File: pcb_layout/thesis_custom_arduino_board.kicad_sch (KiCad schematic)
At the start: 36 parts, among them J1 POWER, J2 USB to TTL, J3 ICSP, J4 VSupply, J5 6-channel Relay, J6 VSupply, J7 Light Sensor, J8 I2C Device, J9 RPi Connector, M1 TXB0104, M2 TB6612FNG, M3 GY-906-BCC, M4 JSN-SR04T, SW1 Reset SW, U1 ATmega328P-P, U2 LM7805, U3 LM317, Y1 16MHz

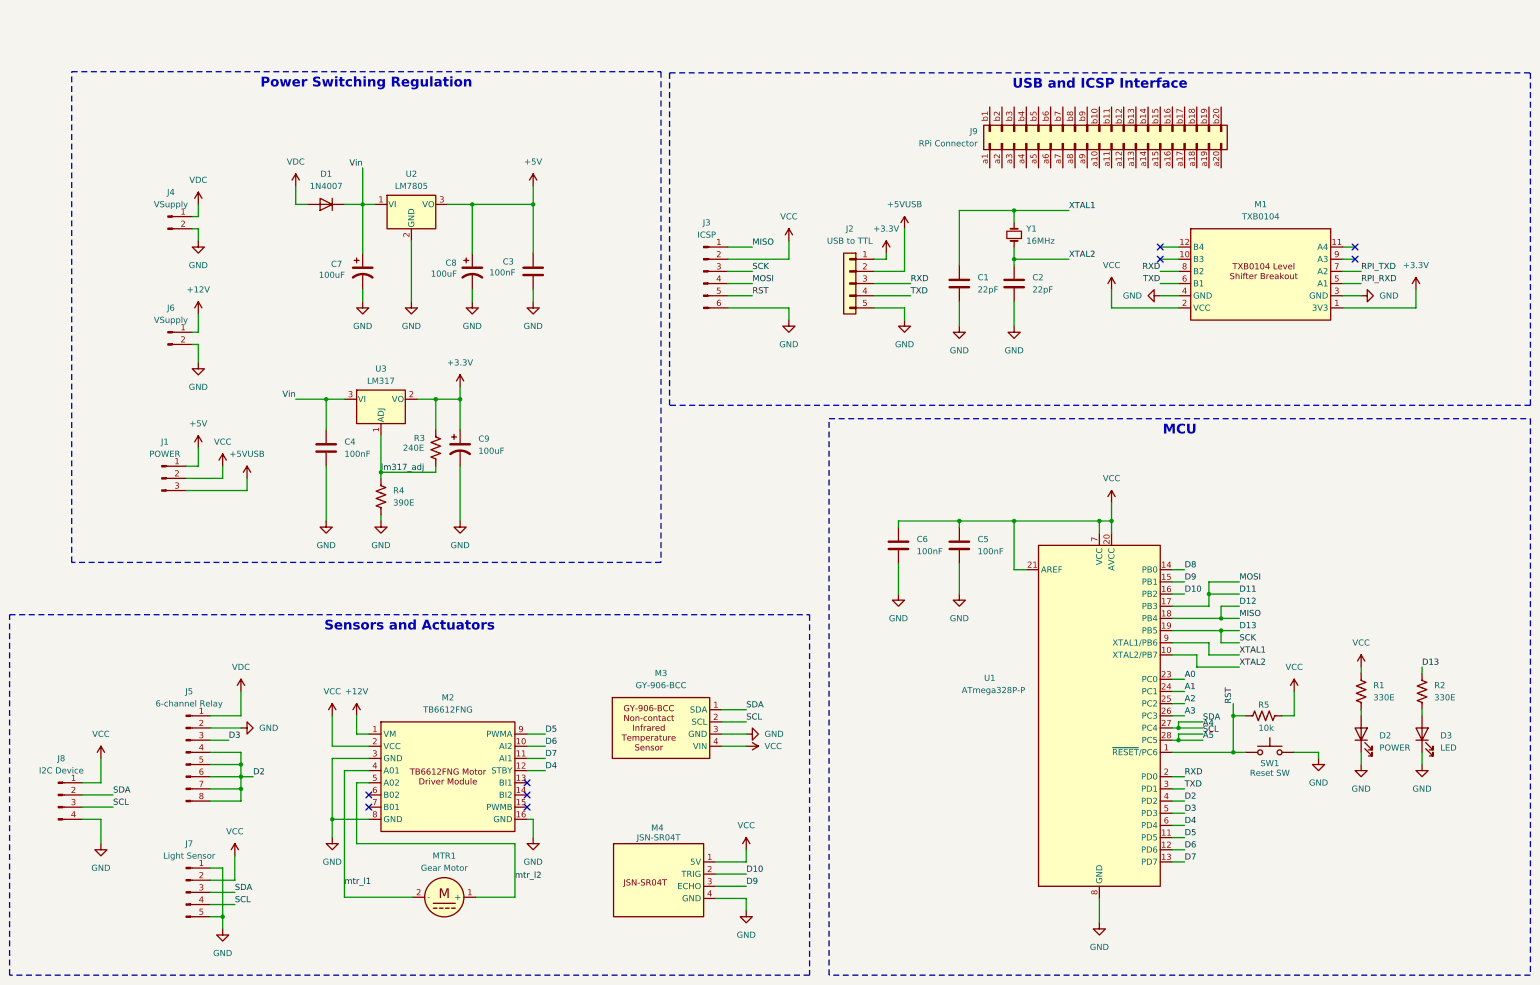
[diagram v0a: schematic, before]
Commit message: Added: Line detector module pins
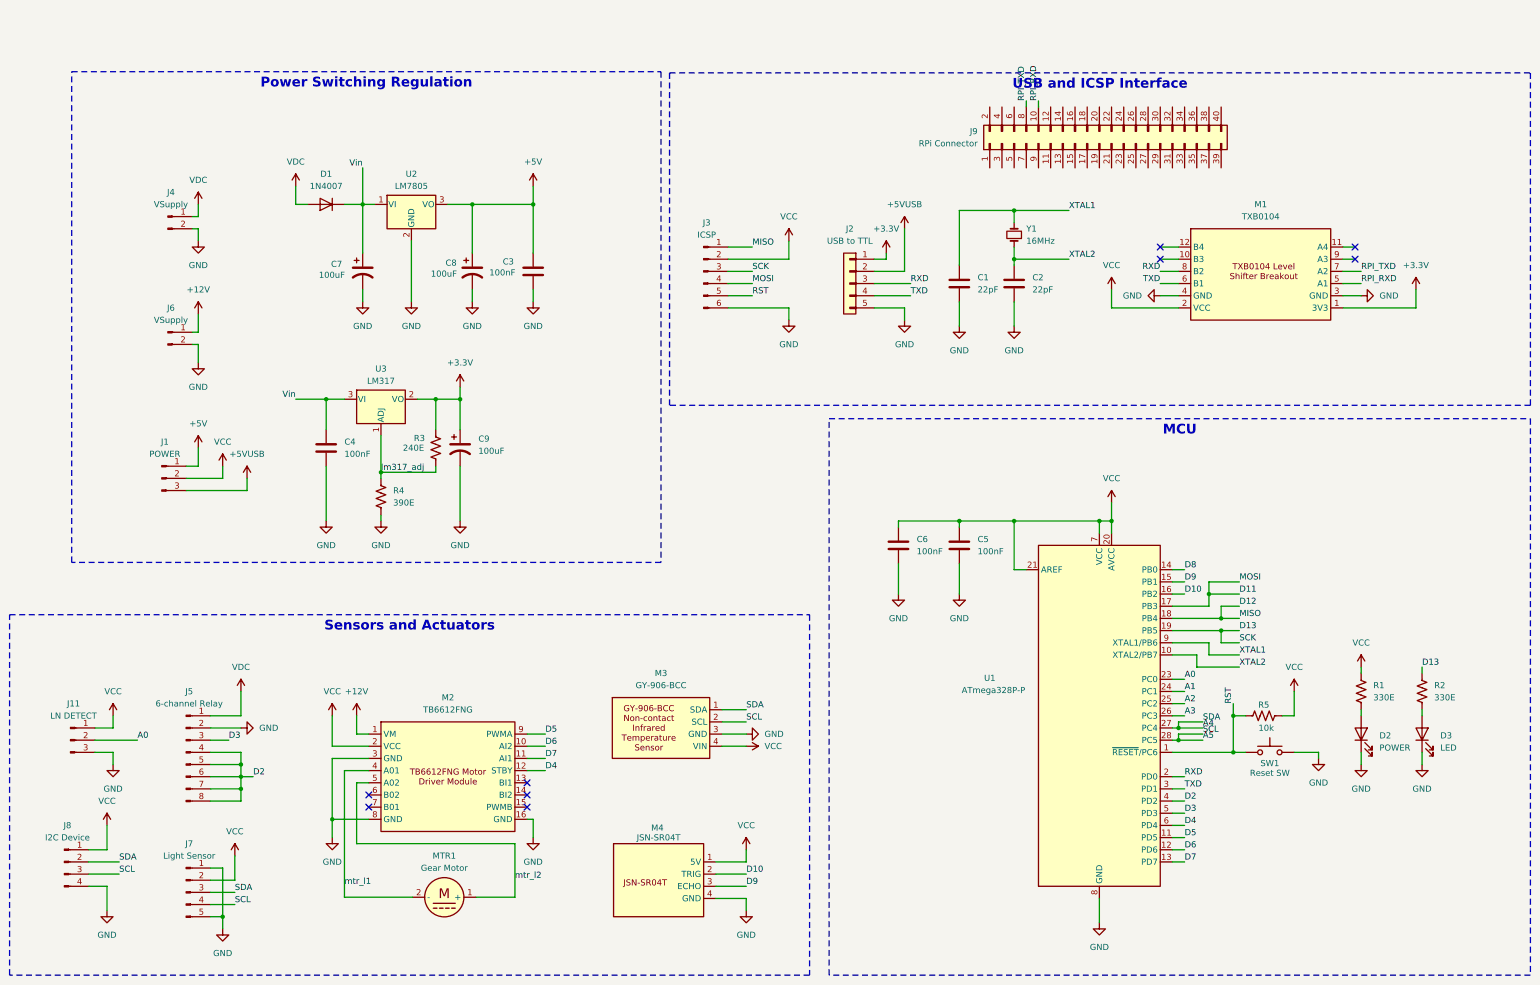
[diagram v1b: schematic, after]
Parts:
- added J11: LN DETECT, Connector_JST:JST_XH_B3B-XH-A_1x03_P2.50mm_Vertical, symbol Connector:Conn_01x03_Pin
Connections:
- net A0: now also J11.2 (Pin_2)
- net GND: now also J11.3 (Pin_3)
- net RPI_RXD: now also J9.10 (Pin_b5)
- net RPI_TXD: now also J9.8 (Pin_b4)
- net VCC: now also J11.1 (Pin_1)
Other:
- moved on the sheet: J8

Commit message: PCB: Added connectors for buttons and fixed connectors
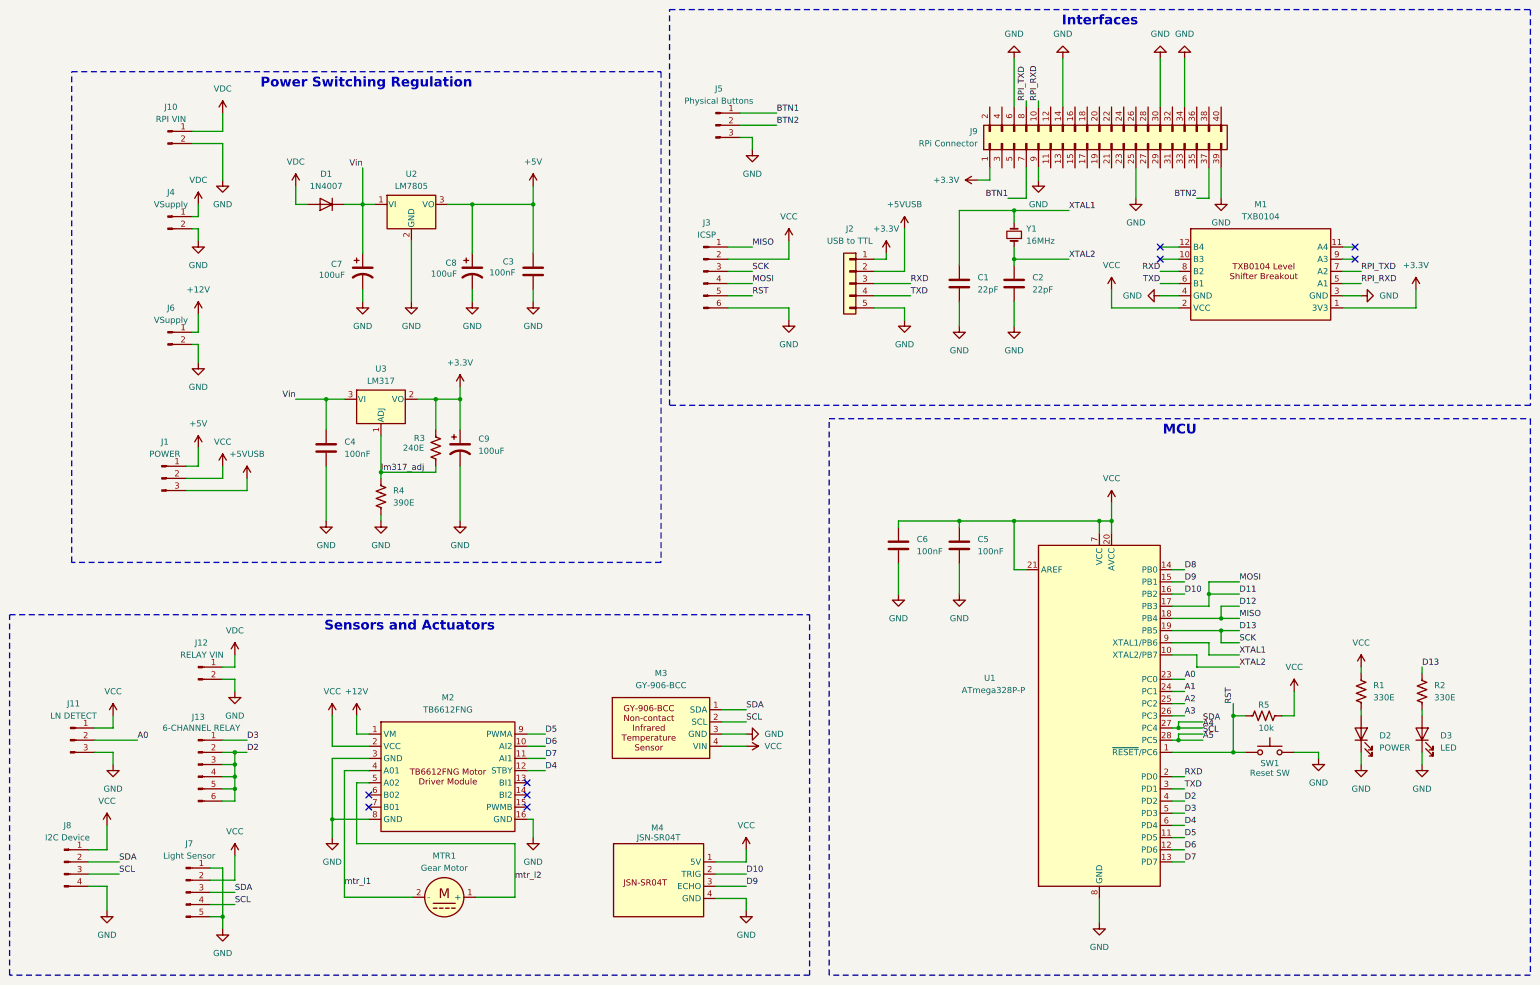
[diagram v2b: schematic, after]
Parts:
- removed J5: 6-channel Relay, Connector_JST:JST_XH_B8B-XH-A_1x08_P2.50mm_Vertical, symbol Connector:Conn_01x08_Pin
- added J10: RPI VIN, Connector_JST:JST_VH_B2P-VH-B_1x02_P3.96mm_Vertical, symbol Connector:Conn_01x02_Pin
- added J12: RELAY VIN, Connector_JST:JST_XH_B2B-XH-A_1x02_P2.50mm_Vertical, symbol Connector:Conn_01x02_Pin
- added J13: 6-CHANNEL RELAY, Connector_JST:JST_XH_B6B-XH-A_1x06_P2.50mm_Vertical, symbol Connector:Conn_01x06_Pin
- added J5: Physical Buttons, Connector_JST:JST_XH_B3B-XH-A_1x03_P2.50mm_Vertical, symbol Connector:Conn_01x03_Pin
- J4: footprint Connector_JST:JST_XH_B2B-XH-A_1x02_P2.50mm_Vertical -> Connector_JST:JST_VH_B2P-VH-B_1x02_P3.96mm_Vertical
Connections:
- net +3.3V: now also J9.1 (2Pin_a1)
- net D2: now also J13.2 (Pin_2), J13.3 (Pin_3), J13.4 (Pin_4), J13.5 (Pin_5), J13.6 (Pin_6)
- net D3: now also J13.1 (Pin_1)
- net GND: now also J9.14 (Pin_b7), J9.25 (Pin_a13), J9.30 (Pin_b15), J9.34 (Pin_b17), J9.39 (Pin_a20), J9.6 (Pin_b3), J9.9 (Pin_a5), J10.2 (Pin_2), J12.2 (Pin_2), J5.3 (Pin_3)
- net VDC: now also J10.1 (Pin_1), J12.1 (Pin_1)
- net BTN2: now reaches J9.37 (Pin_a19)
- net BTN2: now also J5.2 (Pin_2)
- net BTN1: now reaches J9.7 (Pin_a4)
- net BTN1: now also J5.1 (Pin_1)

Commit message: PCB layout: Revision 3.0
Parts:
- added J14: DSI VIN, Connector_JST:JST_XH_B2B-XH-A_1x02_P2.50mm_Vertical, symbol Connector:Conn_01x02_Pin
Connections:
- net GND: now also J14.2 (Pin_2)
- net VDC: now also J14.1 (Pin_1)
- net A1: no longer names the net of U1.24 (PC1)
- net A2: no longer names the net of U1.25 (PC2)
- net A3: no longer names the net of U1.26 (PC3)
- net D8: no longer names the net of U1.14 (PB0)
- no-connect marks 9 -> 41
